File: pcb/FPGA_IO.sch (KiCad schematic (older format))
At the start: 6 parts, among them U4 iCE40-HX8K-CT256, U7 OSC

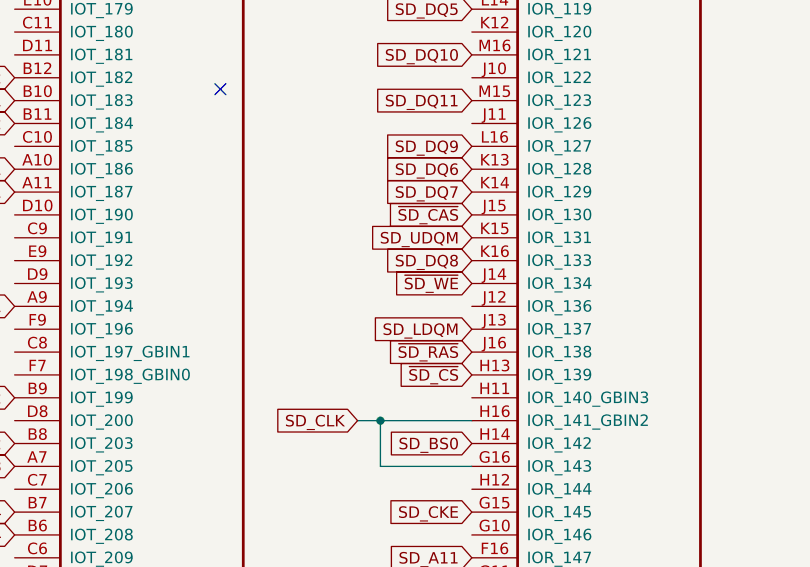
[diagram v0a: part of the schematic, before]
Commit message: Some preliminary routing
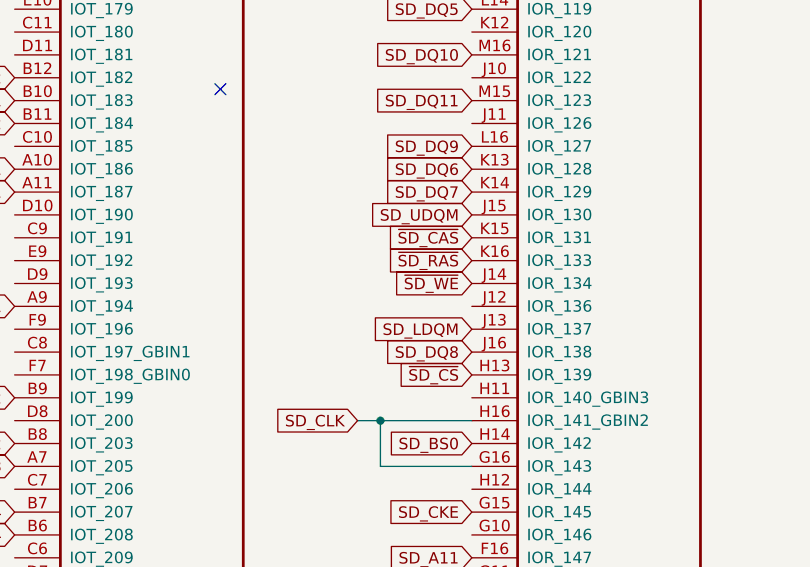
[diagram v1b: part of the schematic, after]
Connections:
- net SD_DQ8: now also U4.J16 (IOR_138); no longer U4.K16 (IOR_133)
- net SD_UDQM: now also U4.J15 (IOR_130); no longer U4.K15 (IOR_131)
- net ~SD_CAS: now also U4.K15 (IOR_131); no longer U4.J15 (IOR_130)
- net ~SD_RAS: now also U4.K16 (IOR_133); no longer U4.J16 (IOR_138)
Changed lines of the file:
@@
 1E 25 49 2A DA F6 C4 5C B7 0C C3 B9 A4 0A 98 09 FC 0D B0 92 CD 57 CD 1F 06 4E 04 26 A7 75 27 49
 52 39 26 13 73 DE C3 6C BE 70 B5 12 F8 16 86 73 8D C3 FF 03 63 F8 EE 2E BE 9A 04 B1 00 00 00 00
-49 45 4E 44 AE 42 60 82 CC
+49 45 4E 44 AE 42 60 82 D3
 EndData
 $EndBitmap
@@
 Text GLabel 3400 2700 0    50   Input ~ 0
 SD_DQ7
-Text GLabel 3400 3000 0    50   Input ~ 0
+Text GLabel 3400 3400 0    50   Input ~ 0
 SD_DQ8
 Text GLabel 3400 2500 0    50   Input ~ 0
@@
 Text GLabel 3400 3300 0    50   Input ~ 0
 SD_LDQM
-Text GLabel 3400 2900 0    50   Input ~ 0
+Text GLabel 3400 2800 0    50   Input ~ 0
 SD_UDQM
 Text GLabel 3400 3100 0    50   Input ~ 0
 ~SD_WE
-Text GLabel 3400 2800 0    50   Input ~ 0
+Text GLabel 3400 2900 0    50   Input ~ 0
 ~SD_CAS
-Text GLabel 3400 3400 0    50   Input ~ 0
+Text GLabel 3400 3000 0    50   Input ~ 0
 ~SD_RAS
 Text GLabel 3400 3500 0    50   Input ~ 0

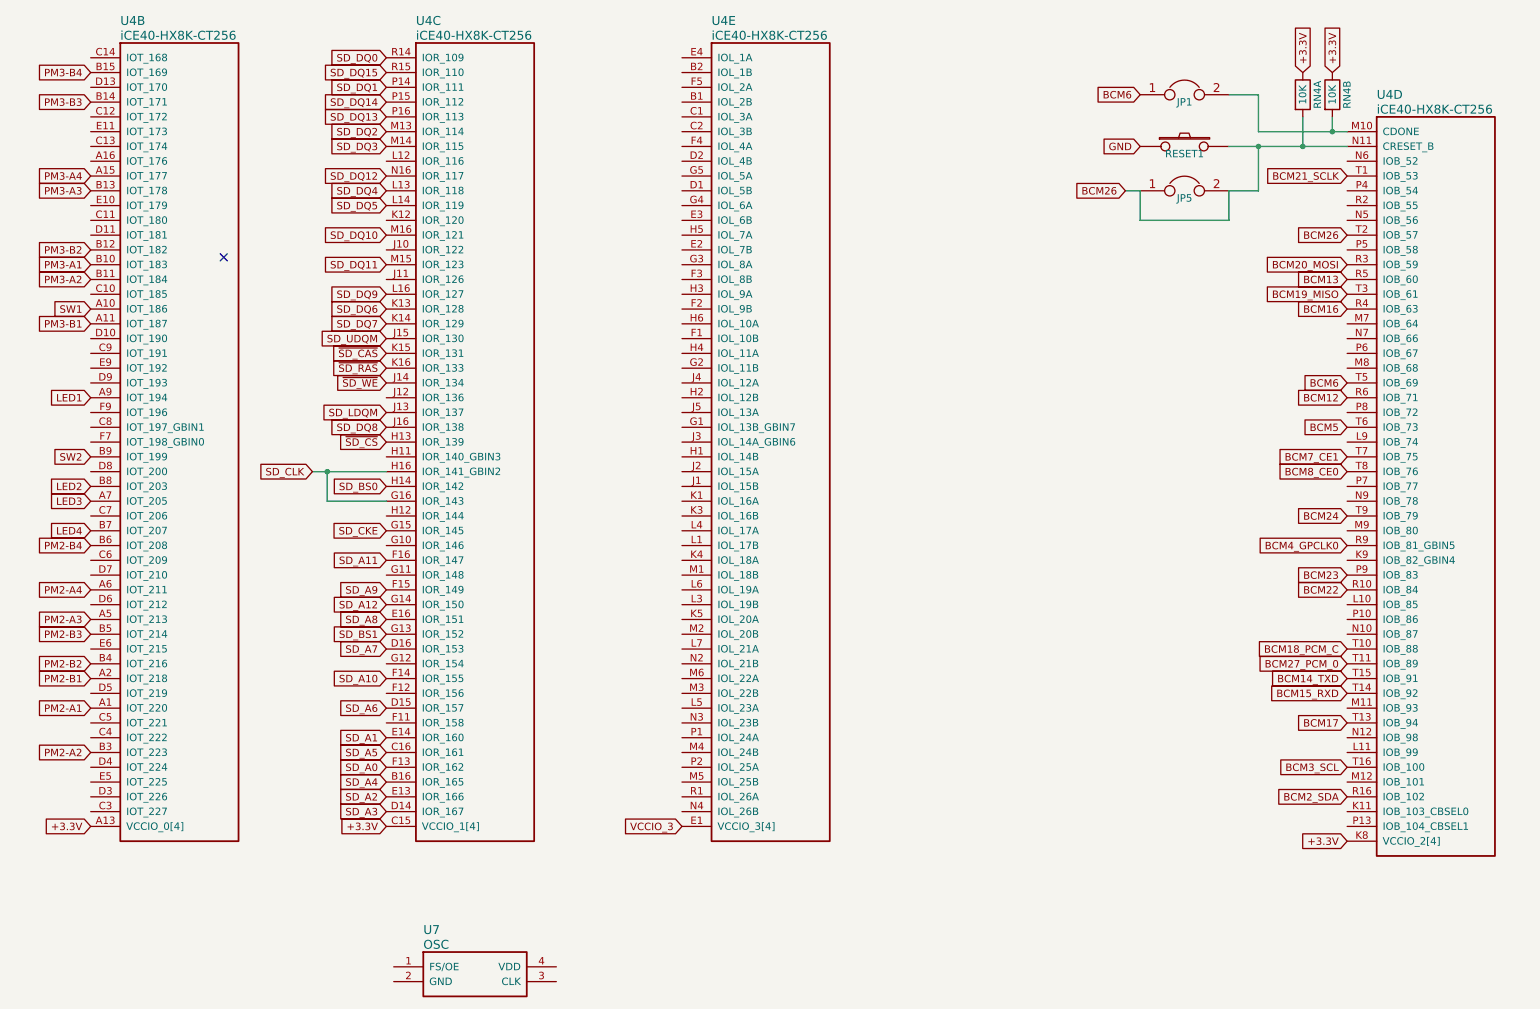
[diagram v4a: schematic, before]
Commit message: SDRAM & BGA are on the board. * Lots of routing.
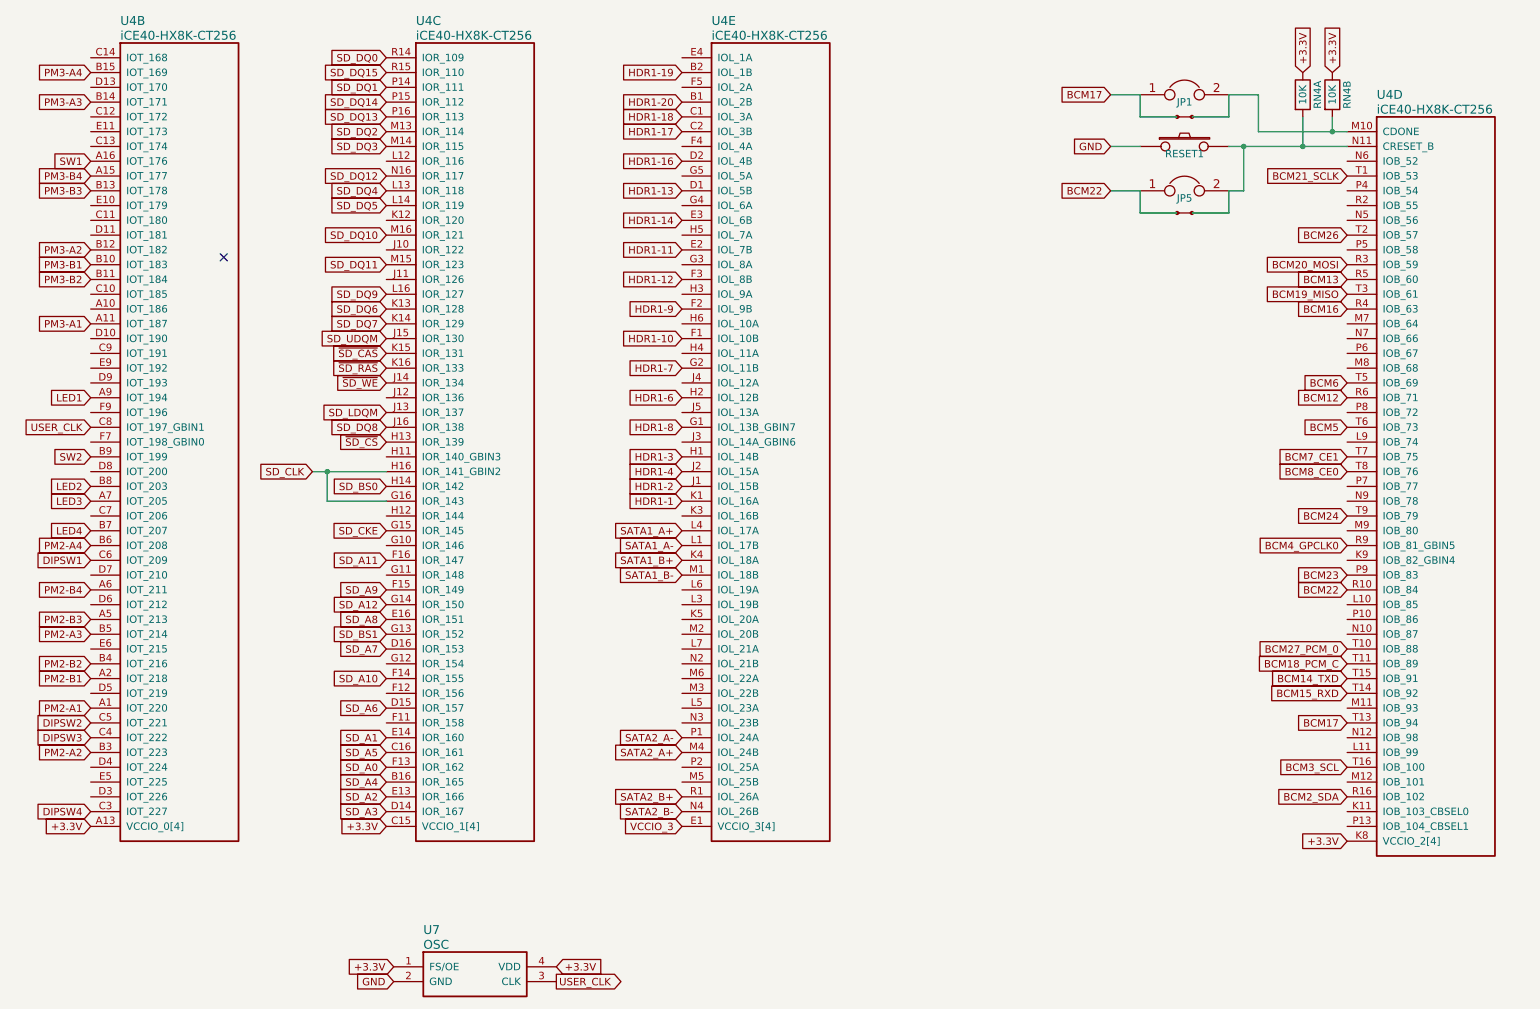
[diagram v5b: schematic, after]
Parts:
- added J2, J3: JSHORTNORMAL, XESS:xess-JSHORT, symbol JSHORTNORMAL
- U7: manf# (none) -> 501ACA100M000CAG
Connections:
- net +3.3V: now also U7.1 (FS/OE), U7.4 (VDD)
- net BCM17: now also JP1.1, J2.2
- net BCM18_PCM_C: now also U4.T11 (IOB_89); no longer U4.T10 (IOB_88)
- net BCM22: now also JP5.1, J3.2
- net BCM26: no longer JP5.1, JP5.2, RESET1.2, RN4.1, U4.N11 (CRESET_B)
- net BCM27_PCM_0: now also U4.T10 (IOB_88); no longer U4.T11 (IOB_89)
- net BCM6: no longer JP1.1
- net GND: now also U7.2 (GND)
- net PM2-A3: now also U4.B5 (IOT_214); no longer U4.A5 (IOT_213)
- net PM2-A4: now also U4.B6 (IOT_208); no longer U4.A6 (IOT_211)
- net PM2-B3: now also U4.A5 (IOT_213); no longer U4.B5 (IOT_214)
- net PM2-B4: now also U4.A6 (IOT_211); no longer U4.B6 (IOT_208)
- net PM3-A1: now also U4.A11 (IOT_187); no longer U4.B10 (IOT_183)
- net PM3-A2: now also U4.B12 (IOT_182); no longer U4.B11 (IOT_184)
- net PM3-A3: now also U4.B14 (IOT_171); no longer U4.B13 (IOT_178)
- net PM3-A4: now also U4.B15 (IOT_169); no longer U4.A15 (IOT_177)
- net PM3-B1: now also U4.B10 (IOT_183); no longer U4.A11 (IOT_187)
- net PM3-B2: now also U4.B11 (IOT_184); no longer U4.B12 (IOT_182)
- net PM3-B3: now also U4.B13 (IOT_178); no longer U4.B14 (IOT_171)
- net PM3-B4: now also U4.A15 (IOT_177); no longer U4.B15 (IOT_169)
- net SW1: now also U4.A16 (IOT_176); no longer U4.A10 (IOT_186)
- net DIPSW4: now reaches U4.C3 (IOT_227)
- net DIPSW3: now reaches U4.C4 (IOT_222)
- net DIPSW2: now reaches U4.C5 (IOT_221)
- net DIPSW1: now reaches U4.C6 (IOT_209)
- net USER_CLK: now reaches U4.C8 (IOT_197_GBIN1)
- net USER_CLK: now also U7.3 (CLK)
- net at JP1.2, RN4.2, U4.M10 (CDONE): now also J2.1
- net HDR1-20: now reaches U4.B1 (IOL_2B)
- net HDR1-19: now reaches U4.B2 (IOL_1B)
- net HDR1-18: now reaches U4.C1 (IOL_3A)
- net HDR1-17: now reaches U4.C2 (IOL_3B)
- net HDR1-13: now reaches U4.D1 (IOL_5B)
- net HDR1-16: now reaches U4.D2 (IOL_4B)
- net HDR1-11: now reaches U4.E2 (IOL_7B)
- net HDR1-14: now reaches U4.E3 (IOL_6B)
- net HDR1-10: now reaches U4.F1 (IOL_10B)
- net HDR1-9: now reaches U4.F2 (IOL_9B)
- net HDR1-12: now reaches U4.F3 (IOL_8B)
- net HDR1-8: now reaches U4.G1 (IOL_13B_GBIN7)
- net HDR1-7: now reaches U4.G2 (IOL_11B)
- net HDR1-3: now reaches U4.H1 (IOL_14B)
- net HDR1-6: now reaches U4.H2 (IOL_12B)
- net HDR1-2: now reaches U4.J1 (IOL_15B)
- net HDR1-4: now reaches U4.J2 (IOL_15A)
- net HDR1-1: now reaches U4.K1 (IOL_16A)
- net SATA1_B+: now reaches U4.K4 (IOL_18A)
- net SATA1_A-: now reaches U4.L1 (IOL_17B)
- net SATA1_A+: now reaches U4.L4 (IOL_17A)
- net SATA1_B-: now reaches U4.M1 (IOL_18B)
- net SATA2_A+: now reaches U4.M4 (IOL_24B)
- net SATA2_B-: now reaches U4.N4 (IOL_26B)
- net SATA2_A-: now reaches U4.P1 (IOL_24A)
- net SATA2_B+: now reaches U4.R1 (IOL_26A)
- new net: J3.1, JP5.2, RESET1.2, RN4.1, U4.N11 (CRESET_B)
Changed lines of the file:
@@
 1E 25 49 2A DA F6 C4 5C B7 0C C3 B9 A4 0A 98 09 FC 0D B0 92 CD 57 CD 1F 06 4E 04 26 A7 75 27 49
 52 39 26 13 73 DE C3 6C BE 70 B5 12 F8 16 86 73 8D C3 FF 03 63 F8 EE 2E BE 9A 04 B1 00 00 00 00
-49 45 4E 44 AE 42 60 82 89
+49 45 4E 44 AE 42 60 82 46
 EndData
 $EndBitmap
@@
 F 2 "XESS:2.5x3.2" H 3450 7050 50  0001 C CNN
 F 3 "" H 3450 7050 50  0000 C CNN
+F 4 "501ACA100M000CAG" H 3450 7050 60  0001 C CNN "manf#"
 	1    3450 7050
 	1    0    0    -1
@@
 Wire Wire Line
 	9800 1400 9800 1300
-Wire Wire Line
-	9600 1500 9600 1300
-Wire Wire Line
-	9100 1500 9900 1500
 Connection ~ 9800 1400
-Connection ~ 9600 1500
 Text GLabel 9600 1000 1    50   Input ~ 0
 +3.3V
@@
 Text GLabel 9900 4500 0    50   Input ~ 0
 BCM22
-Text GLabel 9900 5000 0    50   Input ~ 0
+Text GLabel 9900 4900 0    50   Input ~ 0
 BCM27_PCM_0
 Text GLabel 9900 5400 0    50   Input ~ 0
@@
 Text GLabel 9900 5200 0    50   Input ~ 0
 BCM15_RXD
-Text GLabel 9900 4900 0    50   Input ~ 0
+Text GLabel 9900 5000 0    50   Input ~ 0
 BCM18_PCM_C
 Text GLabel 9900 4400 0    50   Input ~ 0
@@
 Text GLabel 1400 5000 0    50   Input ~ 0
 PM2-B2
+Text GLabel 1400 4800 0    50   Input ~ 0
+PM2-A3
 Text GLabel 1400 4700 0    50   Input ~ 0
-PM2-A3
-Text GLabel 1400 4800 0    50   Input ~ 0
 PM2-B3
+Text GLabel 1400 4200 0    50   Input ~ 0
+PM2-A4
 Text GLabel 1400 4500 0    50   Input ~ 0
-PM2-A4
-Text GLabel 1400 4200 0    50   Input ~ 0
 PM2-B4
+Text GLabel 1400 2300 0    50   Input ~ 0
+PM3-B1
+Text GLabel 1400 2200 0    50   Input ~ 0
+PM3-A2
+Text GLabel 1400 2400 0    50   Input ~ 0
+PM3-B2
+Text GLabel 1400 1200 0    50   Input ~ 0
+PM3-A3
+Text GLabel 1400 1800 0    50   Input ~ 0
+PM3-B3
+Text GLabel 1400 1000 0    50   Input ~ 0
+PM3-A4
+Text GLabel 1400 1700 0    50   Input ~ 0
+PM3-B4
 Text GLabel 1400 2700 0    50   Input ~ 0
-PM3-B1
-Text GLabel 1400 2400 0    50   Input ~ 0
-PM3-A2
-Text GLabel 1400 2200 0    50   Input ~ 0
-PM3-B2
-Text GLabel 1400 1800 0    50   Input ~ 0
-PM3-A3
-Text GLabel 1400 1200 0    50   Input ~ 0
-PM3-B3
-Text GLabel 1400 1700 0    50   Input ~ 0
-PM3-A4
-Text GLabel 1400 1000 0    50   Input ~ 0
-PM3-B4
-Text GLabel 1400 2300 0    50   Input ~ 0
 PM3-A1
 $Comp
@@
 	1    0    0    -1
 $EndComp
-Text GLabel 8500 1500 0    50   Input ~ 0
+Text GLabel 8300 1500 0    50   Input ~ 0
 GND
-Wire Wire Line
-	9300 1500 9300 1800
-Wire Wire Line
-	9300 1800 9100 1800
-Connection ~ 9300 1500
-Text GLabel 8400 1800 0    50   Input ~ 0
-BCM26
 $Comp
 L JUMPER JP5
@@
 Wire Wire Line
 	9300 1150 9100 1150
-Text GLabel 8500 1150 0    50   Input ~ 0
-BCM6
+Text GLabel 8300 1150 0    50   Input ~ 0
+BCM17
 Text GLabel 9800 1000 1    50   Input ~ 0
 +3.3V
@@
 Text GLabel 1400 6100 0    50   Input ~ 0
 +3.3V
-Text GLabel 1400 2600 0    50   Input ~ 0
-SW1
 Text GLabel 1400 3600 0    50   Input ~ 0
 SW2
@@
 Text GLabel 1400 4100 0    50   Input ~ 0
 LED4
-Wire Wire Line
-	8500 1800 8400 1800
-Wire Wire Line
-	8500 1800 8500 2000
-Wire Wire Line
-	8500 2000 9100 2000
-Wire Wire Line
-	9100 2000 9100 1800
+Text GLabel 1400 6000 0    50   Input ~ 0
+DIPSW4
+Text GLabel 1400 5500 0    50   Input ~ 0
+DIPSW3
+Text GLabel 1400 5400 0    50   Input ~ 0
+DIPSW2
+Text GLabel 1400 4300 0    50   Input ~ 0
+DIPSW1
+Text GLabel 1400 1600 0    50   Input ~ 0
+SW1
+Text GLabel 5400 4100 0    50   Input ~ 0
+SATA1_A+
+Text GLabel 5400 4200 0    50   Input ~ 0
+SATA1_A-
+Text GLabel 5400 4300 0    50   Input ~ 0
+SATA1_B+
+Text GLabel 5400 4400 0    50   Input ~ 0
+SATA1_B-
+Text GLabel 5400 5600 0    50   Input ~ 0
+SATA2_A+
+Text GLabel 5400 5500 0    50   Input ~ 0
+SATA2_A-
+Text GLabel 5400 5900 0    50   Input ~ 0
+SATA2_B+
+Text GLabel 5400 6000 0    50   Input ~ 0
+SATA2_B-
+Text GLabel 5400 3900 0    50   Input ~ 0
+HDR1-1
+Text GLabel 5400 3700 0    50   Input ~ 0
+HDR1-4
+Text GLabel 5400 3000 0    50   Input ~ 0
+HDR1-7
+Text GLabel 5400 3800 0    50   Input ~ 0
+HDR1-2
+Text GLabel 5400 3600 0    50   Input ~ 0
+HDR1-3
+Text GLabel 5400 3200 0    50   Input ~ 0
+HDR1-6
+Text GLabel 5400 3400 0    50   Input ~ 0
+HDR1-8
+Text GLabel 5400 2400 0    50   Input ~ 0
+HDR1-12
+Text GLabel 5400 2600 0    50   Input ~ 0
+HDR1-9
+Text GLabel 5400 1800 0    50   Input ~ 0
+HDR1-13
+Text GLabel 5400 1300 0    50   Input ~ 0
+HDR1-18
+Text GLabel 5400 1000 0    50   Input ~ 0
+HDR1-19
+Text GLabel 5400 1200 0    50   Input ~ 0
+HDR1-20
+Text GLabel 5400 1400 0    50   Input ~ 0
+HDR1-17
+Text GLabel 5400 1600 0    50   Input ~ 0
+HDR1-16
+Text GLabel 5400 2200 0    50   Input ~ 0
+HDR1-11
+Text GLabel 5400 2800 0    50   Input ~ 0
+HDR1-10
+Text GLabel 5400 2000 0    50   Input ~ 0
+HDR1-14
+Text GLabel 4550 7050 2    50   Input ~ 0
++3.3V
+Text GLabel 3450 7050 0    50   Input ~ 0
++3.3V
+Text GLabel 3450 7150 0    50   Input ~ 0
+GND
+Text GLabel 4550 7150 2    50   Output ~ 0
+USER_CLK
+Text GLabel 1400 3400 0    50   Input ~ 0
+USER_CLK
+Wire Wire Line
+	9900 1500 9100 1500
+Wire Wire Line
+	9600 1300 9600 1500
+Connection ~ 9600 1500
+Wire Wire Line
+	9100 1800 9200 1800
+Wire Wire Line
+	9200 1800 9200 1500
+Connection ~ 9200 1500
+Text GLabel 8300 1800 0    50   Input ~ 0
+BCM22
+$Comp
+L JSHORTNORMAL J?
+U 1 1 55F913D4
+P 8850 1300
+AR Path="/55F913D4" Ref="J?"  Part="1"
+AR Path="/55DF5F27/55E883EA/55F049F2/55F913D4" Ref="J2"  Part="1"
+F 0 "J2" H 8850 1200 50  0001 L BNN
+F 1 "JSHORTNORMAL" H 8750 1200 50  0001 L BNN
+F 2 "XESS:xess-JSHORT" H 8850 1450 50  0001 C CNN
+F 3 "" H 8850 1300 60  0000 C CNN
+	1    8850 1300
+	-1   0    0    1
+$EndComp
+$Comp
+L JSHORTNORMAL J?
+U 1 1 55F913E4
+P 8850 1950
+AR Path="/55F913E4" Ref="J?"  Part="1"
+AR Path="/55DF5F27/55E883EA/55F049F2/55F913E4" Ref="J3"  Part="1"
+F 0 "J3" H 8850 1850 50  0001 L BNN
+F 1 "JSHORTNORMAL" H 8750 1850 50  0001 L BNN
+F 2 "XESS:xess-JSHORT" H 8850 2100 50  0001 C CNN
+F 3 "" H 8850 1950 60  0000 C CNN
+	1    8850 1950
+	-1   0    0    1
+$EndComp
+Wire Wire Line
+	8500 1150 8300 1150
+Wire Wire Line
+	8500 1500 8300 1500
+Wire Wire Line
+	8500 1800 8300 1800
+Wire Wire Line
+	9100 1150 9100 1300
+Wire Wire Line
+	9100 1300 8850 1300
+Wire Wire Line
+	8750 1300 8500 1300
+Wire Wire Line
+	8500 1300 8500 1150
+Wire Wire Line
+	8500 1800 8500 1950
+Wire Wire Line
+	8500 1950 8750 1950
+Wire Wire Line
+	8850 1950 9100 1950
+Wire Wire Line
+	9100 1950 9100 1800
 $EndSCHEMATC

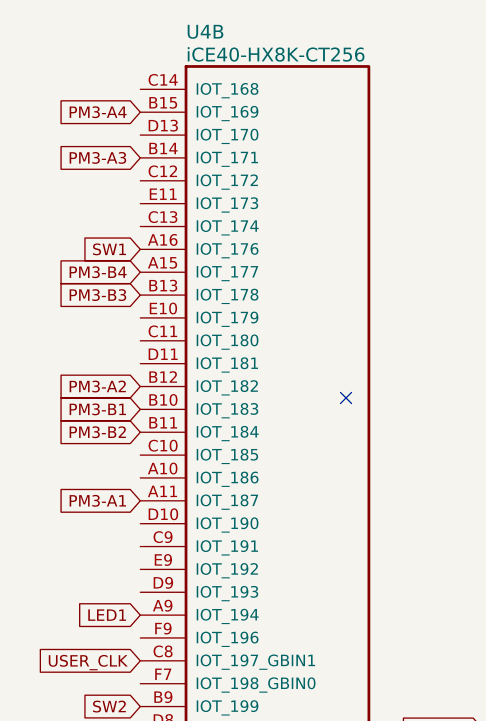
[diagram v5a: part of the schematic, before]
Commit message: Split power planes built. * Capacitors approximately placed.
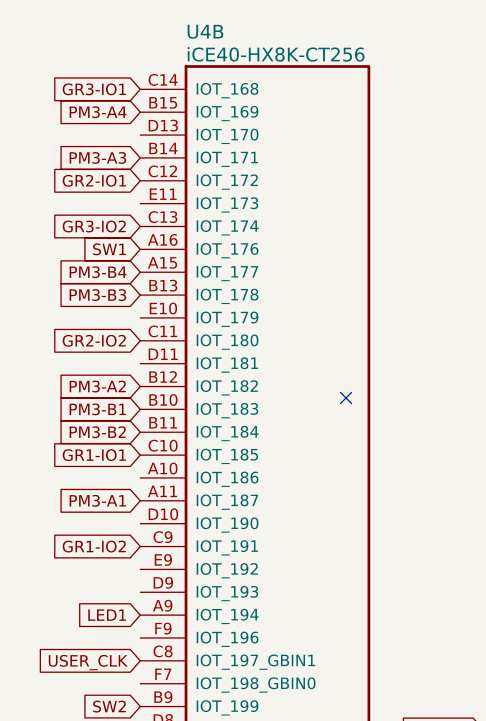
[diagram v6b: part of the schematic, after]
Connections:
- net GR1-IO1: now reaches U4.C10 (IOT_185)
- net GR2-IO2: now reaches U4.C11 (IOT_180)
- net GR2-IO1: now reaches U4.C12 (IOT_172)
- net GR3-IO2: now reaches U4.C13 (IOT_174)
- net GR3-IO1: now reaches U4.C14 (IOT_168)
- net GR1-IO2: now reaches U4.C9 (IOT_191)
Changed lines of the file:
@@
 1E 25 49 2A DA F6 C4 5C B7 0C C3 B9 A4 0A 98 09 FC 0D B0 92 CD 57 CD 1F 06 4E 04 26 A7 75 27 49
 52 39 26 13 73 DE C3 6C BE 70 B5 12 F8 16 86 73 8D C3 FF 03 63 F8 EE 2E BE 9A 04 B1 00 00 00 00
-49 45 4E 44 AE 42 60 82 46
+49 45 4E 44 AE 42 60 82 E6
 EndData
 $EndBitmap
@@
 Wire Wire Line
 	9100 1950 9100 1800
+Text GLabel 1400 2500 0    50   Input ~ 0
+GR1-IO1
+Text GLabel 1400 2900 0    50   Input ~ 0
+GR1-IO2
+Text GLabel 1400 1300 0    50   Input ~ 0
+GR2-IO1
+Text GLabel 1400 2000 0    50   Input ~ 0
+GR2-IO2
+Text GLabel 1400 900  0    50   Input ~ 0
+GR3-IO1
+Text GLabel 1400 1500 0    50   Input ~ 0
+GR3-IO2
 $EndSCHEMATC
